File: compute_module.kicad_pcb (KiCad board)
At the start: 4 copper layers, 93.2 x 62.4 mm, 66 parts, among them J1 2001-1-2-21-00-BK, J2 JC-128, P1 POWER, P2 HOST, P3 CAM1, P4 CONN_02X20, Q1 2N7002P.215, Q2 DMP3056L-7, Q3 2N7002P.215, U1 REG1117-3.3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

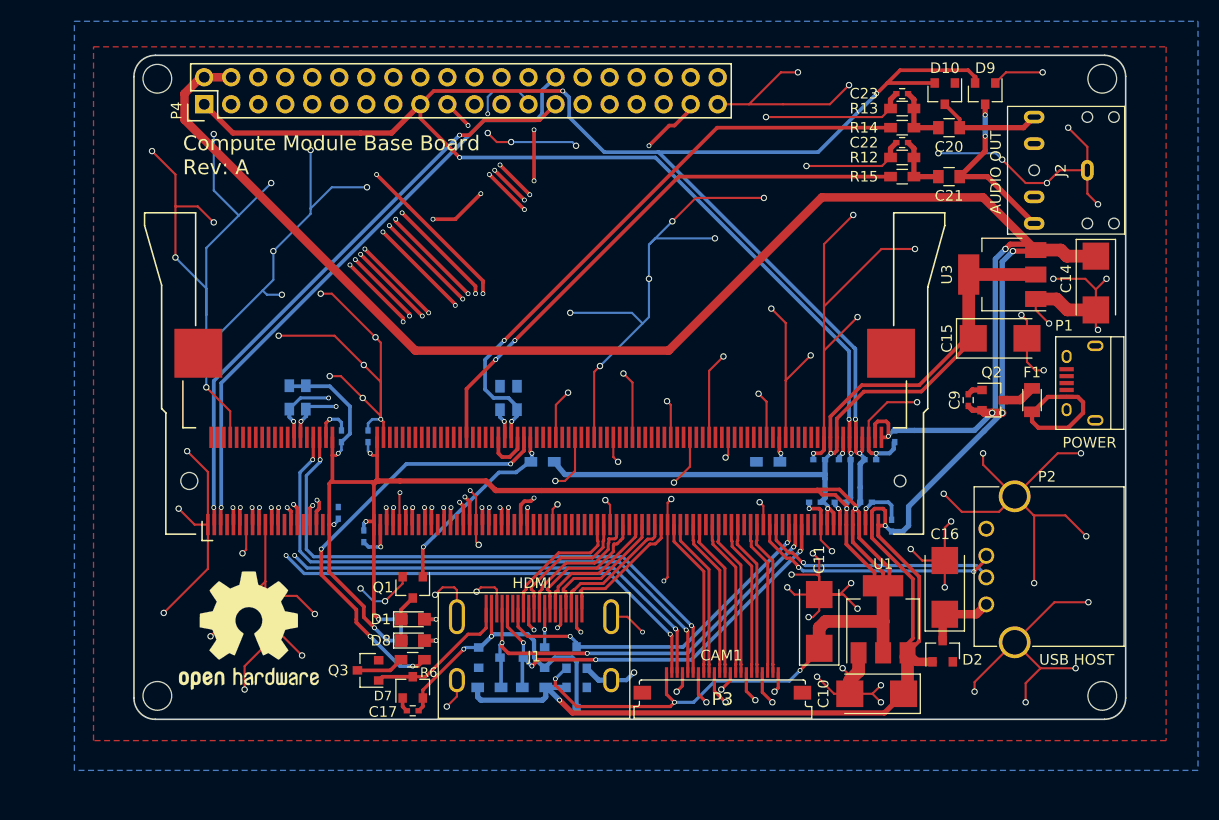
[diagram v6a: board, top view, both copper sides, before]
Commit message: Initial PCB changes to support CAM0+CAM1
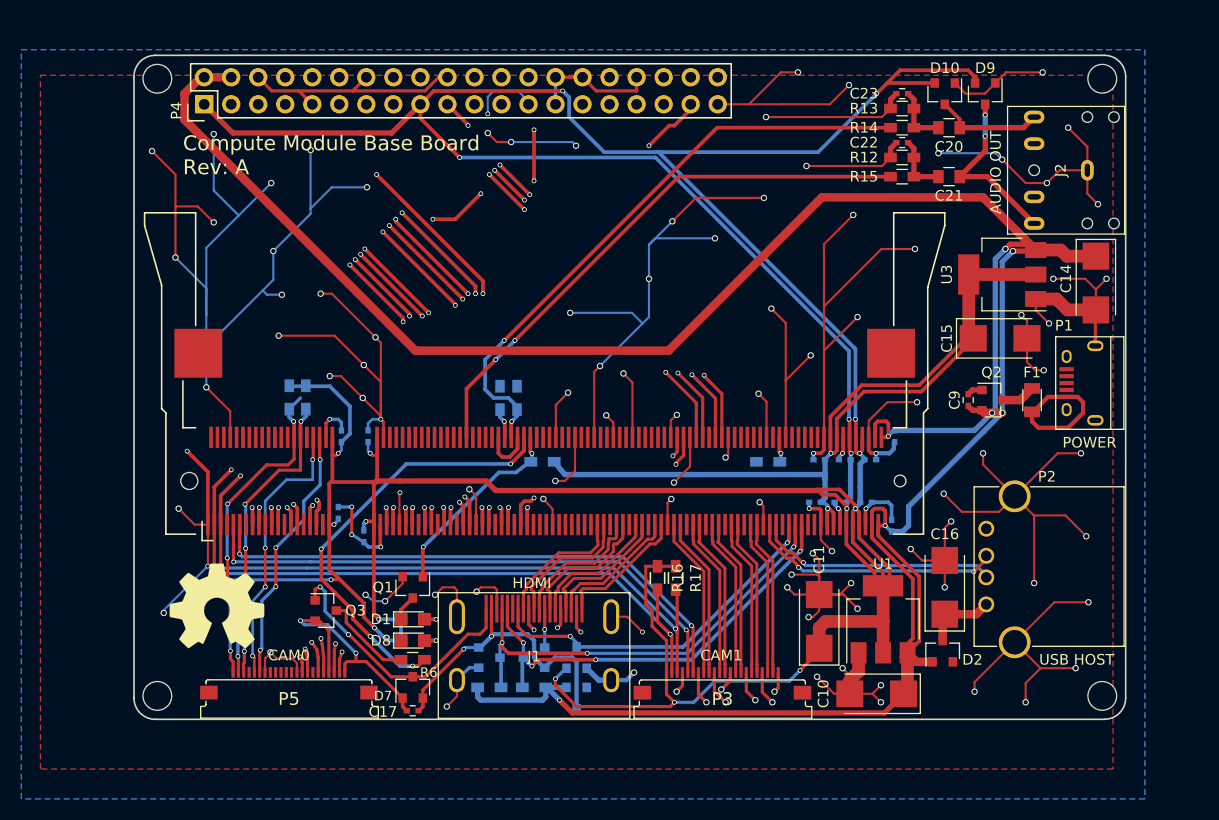
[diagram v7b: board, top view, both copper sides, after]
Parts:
- removed the REF*** at (98.4, 98.0)
- added P5: CAM0, ffc_conn:FPC_22, F.Cu at (102.2, 102.0)
- added R16: 1.8K, Resistors_SMD:R_0603_HandSoldering, F.Cu at (136.8, 93.1)
- added R17: 1.8K, Resistors_SMD:R_0603_HandSoldering, F.Cu at (138.5, 93.1)
- added REF***: OSHW-Symbol_8.9x8mm_SilkScreen, Symbols:OSHW-Symbol_8.9x8mm_SilkScreen, F.Cu at (95.4, 95.8)
- moved Q3 6.89 mm to (105.6, 96.2), turned to 0 degrees
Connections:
- MD1 pad 11: GPIO3 -> CAM1_IO0
- MD1 pad 136: Net-(MD1-Pad136) -> CAM0_D0_P
- MD1 pad 138: Net-(MD1-Pad138) -> CAM0_D0_N
- MD1 pad 142: Net-(MD1-Pad142) -> CAM0_C_P
- MD1 pad 144: Net-(MD1-Pad144) -> CAM0_C_N
- MD1 pad 148: Net-(MD1-Pad148) -> CAM0_D1_P
- MD1 pad 150: Net-(MD1-Pad150) -> CAM0_D1_N
- MD1 pad 28: CD1_SDA -> CD0_SDA
- MD1 pad 3: GPIO0 -> CD1_SDA
- MD1 pad 30: CD1_SCL -> CD0_SCL
- MD1 pad 34: CAM1_IO1 -> CAM0_IO1
- MD1 pad 36: CAM1_IO0 -> CAM0_IO0
- MD1 pad 5: GPIO1 -> CD1_SCL
- MD1 pad 9: GPIO2 -> CAM1_IO1
- P4 pad 27: GPIO0 -> GND
- P4 pad 28: GPIO1 -> GND
- P4 pad 3: GPIO2 -> CD1_SDA
- P4 pad 5: GPIO3 -> CD1_SCL
- R10 pad 2: CD1_SCL -> CD0_SCL
- R9 pad 2: CD1_SDA -> CD0_SDA
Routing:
- net CAM0_C_P: track 0.00 -> 64.5 mm, vias 0 -> 2
- net CAM0_C_N: track 0.00 -> 63.8 mm, vias 0 -> 2
- net CAM0_D1_P: track 0.00 -> 63.2 mm, vias 0 -> 2
- net CAM0_D1_N: track 0.00 -> 61.6 mm, vias 0 -> 2
- net GPIO1: track 57.9 -> 0.00 mm, vias 1 -> 0
- net GPIO0: track 56.4 -> 0.00 mm, vias 2 -> 0
- net CAM0_D0_P: track 0.00 -> 47.0 mm, vias 0 -> 2
- net CAM0_D0_N: track 0.00 -> 47.0 mm, vias 0 -> 2
- net GPIO3: track 40.2 -> 0.00 mm, vias 1 -> 0
- net GPIO2: track 39.6 -> 0.00 mm, vias 1 -> 0
- net +3V3: track 386.1 -> 420.5 mm, vias 18 -> 20
- net CD1_SCL: track 67.3 -> 98.4 mm, vias 4 -> 3
- net CD0_SDA: track 0.00 -> 30.5 mm, vias 0 -> 5
- net CD0_SCL: track 0.00 -> 28.7 mm, vias 0 -> 5
- net CD1_SDA: track 69.5 -> 98.0 mm, vias 4 -> 3
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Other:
- board text added: "CAM0"
